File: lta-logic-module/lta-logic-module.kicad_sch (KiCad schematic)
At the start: 14 parts

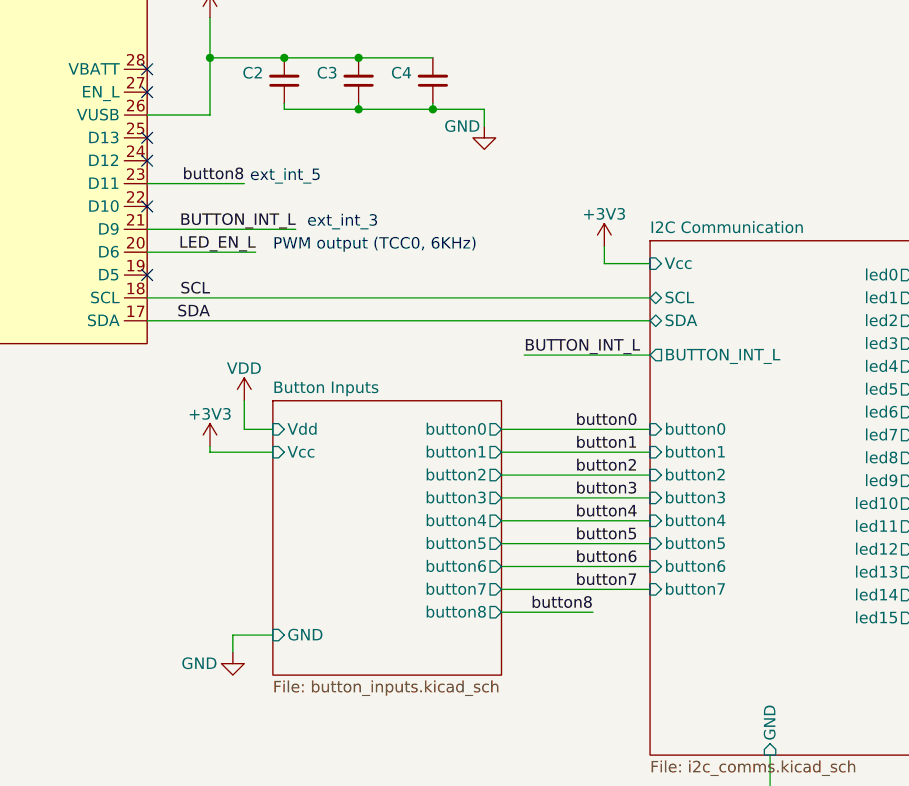
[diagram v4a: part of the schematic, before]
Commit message: Relocated optosensor to south side of board.
* Moved optosensor logic away from the USB plug-side of the Feather.
  You can now plug in USB while the Feather is attached to the board.
* Changed schematic such that `button0` now goes directly to the
  Feather; buttons 1--8 are on the I2C bus. Cleans up some obnoxious
  routing.
* Optimized other routing & GND fill.
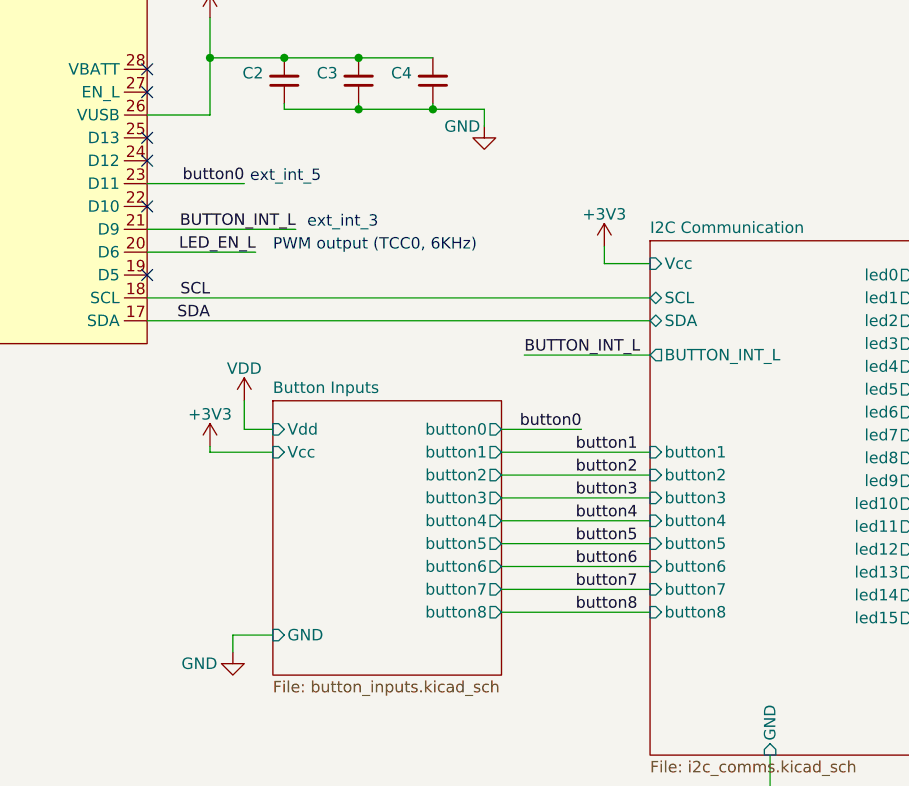
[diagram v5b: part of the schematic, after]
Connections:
- net button0: now also U1.23 (D11)
- net button8: no longer U1.23 (D11)
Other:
- sheet I2C Communication ports: added button8; removed button0
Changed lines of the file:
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@@
-    (stroke (width 0) (type default) (color 0 0 0 0))
-  )
-  (wire (pts (xy 132.715 111.76) (xy 149.225 111.76))
     (stroke (width 0) (type default) (color 0 0 0 0))
   )
@@
     (stroke (width 0) (type default) (color 0 0 0 0))
   )
+  (wire (pts (xy 132.715 111.76) (xy 141.605 111.76))
+    (stroke (width 0) (type default) (color 0 0 0 0))
+  )
   (wire (pts (xy 139.7 171.45) (xy 139.7 179.07))
     (stroke (width 0) (type default) (color 0 0 0 0))
@@
     (stroke (width 0) (type default) (color 0 0 0 0))
   )
-  (wire (pts (xy 132.715 132.08) (xy 142.875 132.08))
+  (wire (pts (xy 132.715 132.08) (xy 149.225 132.08))
     (stroke (width 0) (type default) (color 0 0 0 0))
   )
@@
     (effects (font (size 1.27 1.27)) (justify left bottom))
   )
-  (label "button8" (at 142.875 132.08 180)
+  (label "button8" (at 140.97 132.08 0)
+    (effects (font (size 1.27 1.27)) (justify left bottom))
+  )
+  (label "button0" (at 141.605 111.76 180)
     (effects (font (size 1.27 1.27)) (justify right bottom))
   )
-  (label "button0" (at 140.97 111.76 0)
-    (effects (font (size 1.27 1.27)) (justify left bottom))
-  )
   (label "button2" (at 140.97 116.84 0)
     (effects (font (size 1.27 1.27)) (justify left bottom))
@@
     (effects (font (size 1.27 1.27)) (justify left bottom))
   )
-  (label "button8" (at 104.14 84.455 180)
+  (label "button0" (at 104.14 84.455 180)
     (effects (font (size 1.27 1.27)) (justify right bottom))
   )
@@
       (effects (font (size 1.27 1.27)) (justify left))
     )
-    (pin "button0" input (at 149.225 111.76 180)
-      (effects (font (size 1.27 1.27)) (justify left))
-    )
     (pin "button1" input (at 149.225 114.3 180)
       (effects (font (size 1.27 1.27)) (justify left))
@@
       (effects (font (size 1.27 1.27)) (justify left))
     )
+    (pin "button8" input (at 149.225 132.08 180)
+      (effects (font (size 1.27 1.27)) (justify left))
+    )

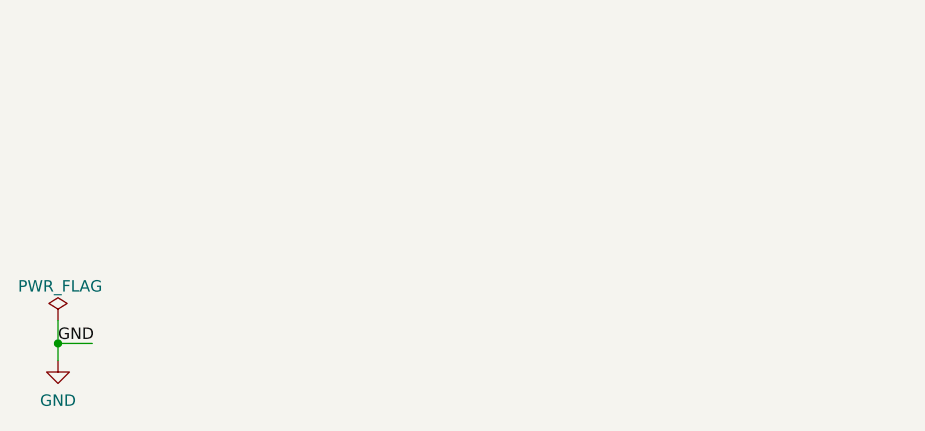
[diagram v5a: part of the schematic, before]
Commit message: Add test points
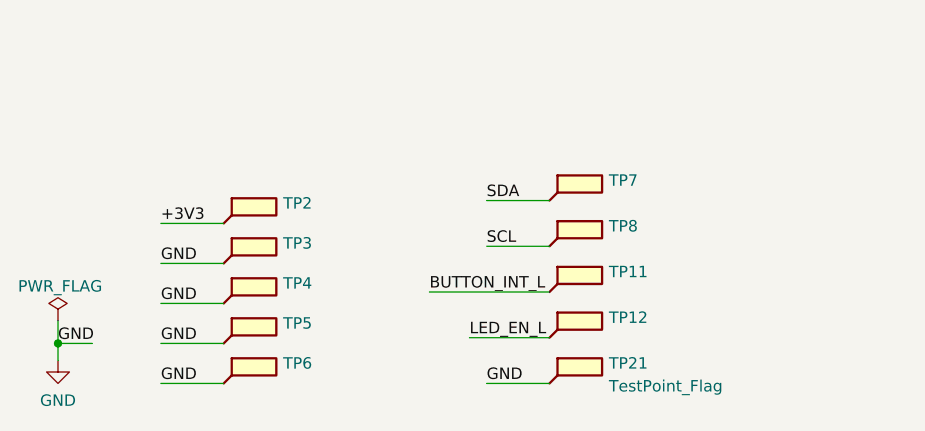
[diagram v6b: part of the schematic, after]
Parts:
- added TP11, TP12, TP2, TP3, TP4, TP5, TP6, TP7, TP8: (no value), symbol Connector:TestPoint_Flag
- added TP21: TestPoint_Flag, Aaron_THT:TestPoint_THTPad_1.0x1.0mm_Drill0.3mm, symbol Connector:TestPoint_Flag
- FID1, FID2, FID3, H1, H2, H3, H4: now left out of the parts list
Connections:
- net +3V3: now also TP2.1
- net BUTTON_INT_L: now also TP11.1
- net GND: now also TP21.1, TP3.1, TP4.1, TP5.1, TP6.1
- net LED_EN_L: now also TP12.1
- net SCL: now also TP8.1
- net SDA: now also TP7.1

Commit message: Final tweaks before RTM.
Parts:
- TP21: value TestPoint_Flag -> (none); footprint Aaron_THT:TestPoint_THTPad_1.0x1.0mm_Drill0.3mm -> (none)
- U1: Comment Use 1x16 and 1x12 female THT headers 2.54mm pitch -> Use 1x16 and 1x12 female THT headers 2.54mm pitch, 6.5--8.0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
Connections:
- net LED_EN_L renamed LED_EN
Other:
- sheet LED Signal Outputs ports: added LED_EN; removed LED_EN_L
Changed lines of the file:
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@@
     (stroke (width 0) (type default) (color 0 0 0 0))
   )
-  (wire (pts (xy 93.345 92.075) (xy 105.41 92.075))
+  (wire (pts (xy 93.345 92.075) (xy 103.505 92.075))
     (stroke (width 0) (type default) (color 0 0 0 0))
   )
@@
     (effects (font (size 1.27 1.27)) (justify left bottom))
   )
-  (label "LED_EN_L" (at 182.245 142.24 0)
+  (label "LED_EN" (at 182.245 142.24 0)
     (effects (font (size 1.27 1.27)) (justify left bottom))
   )
@@
     (effects (font (size 1.27 1.27)) (justify right bottom))
   )
-  (label "LED_EN_L" (at 63.5 189.865 0)
+  (label "LED_EN" (at 63.5 189.865 0)
     (effects (font (size 1.27 1.27)) (justify left bottom))
   )
@@
     (effects (font (size 1.27 1.27)) (justify left bottom))
   )
-  (label "LED_EN_L" (at 105.41 92.075 180)
+  (label "LED_EN" (at 103.505 92.075 180)
     (effects (font (size 1.27 1.27)) (justify right bottom))
   )
@@
       (effects (font (size 1.27 1.27)) (justify left))
     )
-    (property "Value" "TestPoint_Flag" (id 1) (at 78.994 195.2502 0)
-      (effects (font (size 1.27 1.27)) (justify left))
-    )
-    (property "Footprint" "Aaron_THT:TestPoint_THTPad_1.0x1.0mm_Drill0.3mm" (id 2) (at 77.47 194.945 0)
+    (property "Value" "" (id 1) (at 78.994 195.2502 0)
+      (effects (font (size 1.27 1.27)) (justify left))
+    )
+    (property "Footprint" "" (id 2) (at 77.47 194.945 0)
       (effects (font (size 1.27 1.27)) hide)
     )
@@
       (effects (font (size 1.27 1.27)) hide)
     )
-    (property "Comment" "Use 1x16 and 1x12 female THT headers 2.54mm pitch" (id 4) (at 64.135 59.055 0)
+    (property "Comment" "Use 1x16 and 1x12 female THT headers 2.54mm pitch, 6.5--8.0mm tall" (id 4) (at 64.135 59.055 0)
       (effects (font (size 1.27 1.27)) hide)
     )
@@
       (effects (font (size 1.27 1.27)) (justify left))
     )
-    (pin "LED_EN_L" input (at 193.675 142.24 180)
-      (effects (font (size 1.27 1.27)) (justify left))
-    )
+    (pin "LED_EN" input (at 193.675 142.24 180)
+      (effects (font (size 1.27 1.27)) (justify left))
+    )

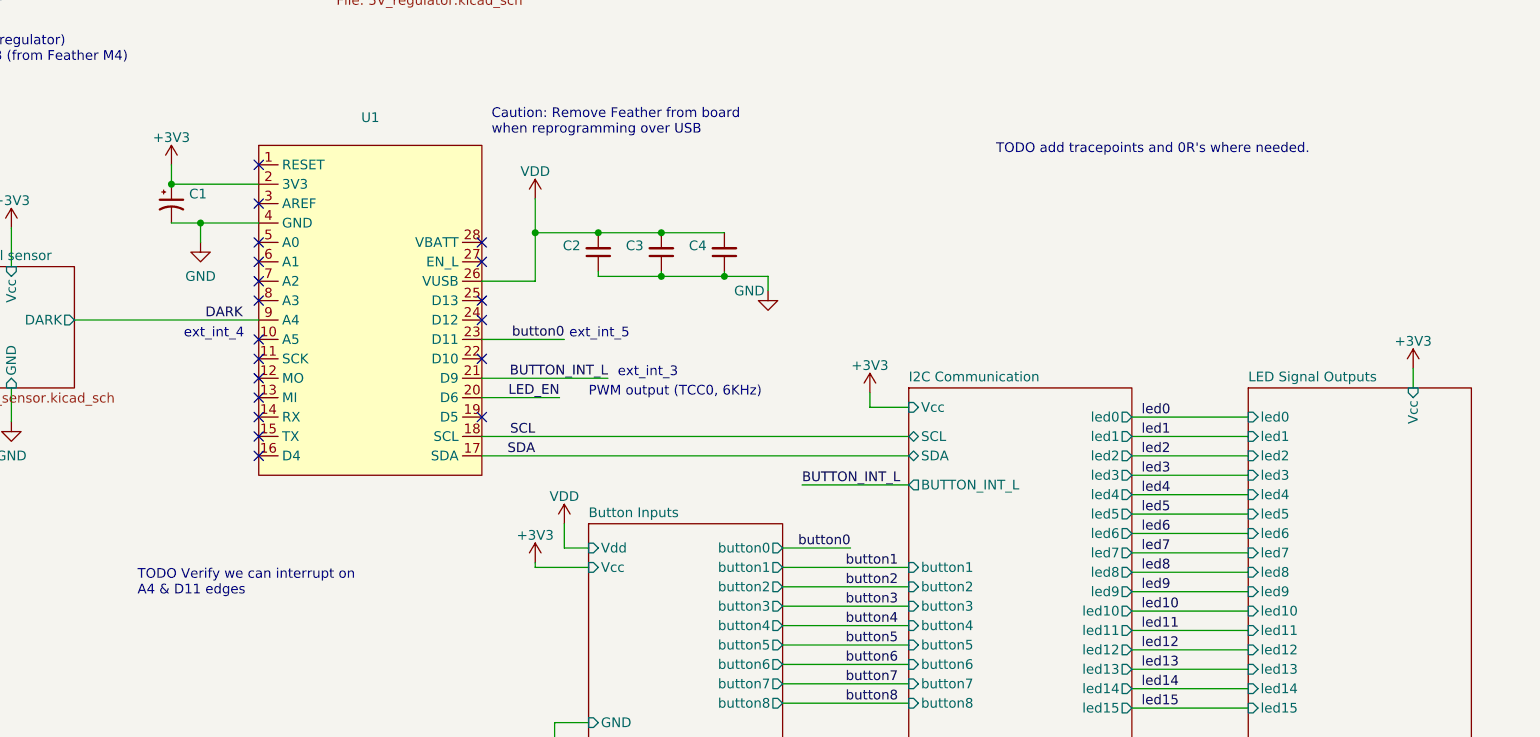
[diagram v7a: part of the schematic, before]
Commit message: Fix GND path return.
* Route power traces over ground plane.
* Add routed corners to edge cuts
* Remove final TODO notes.
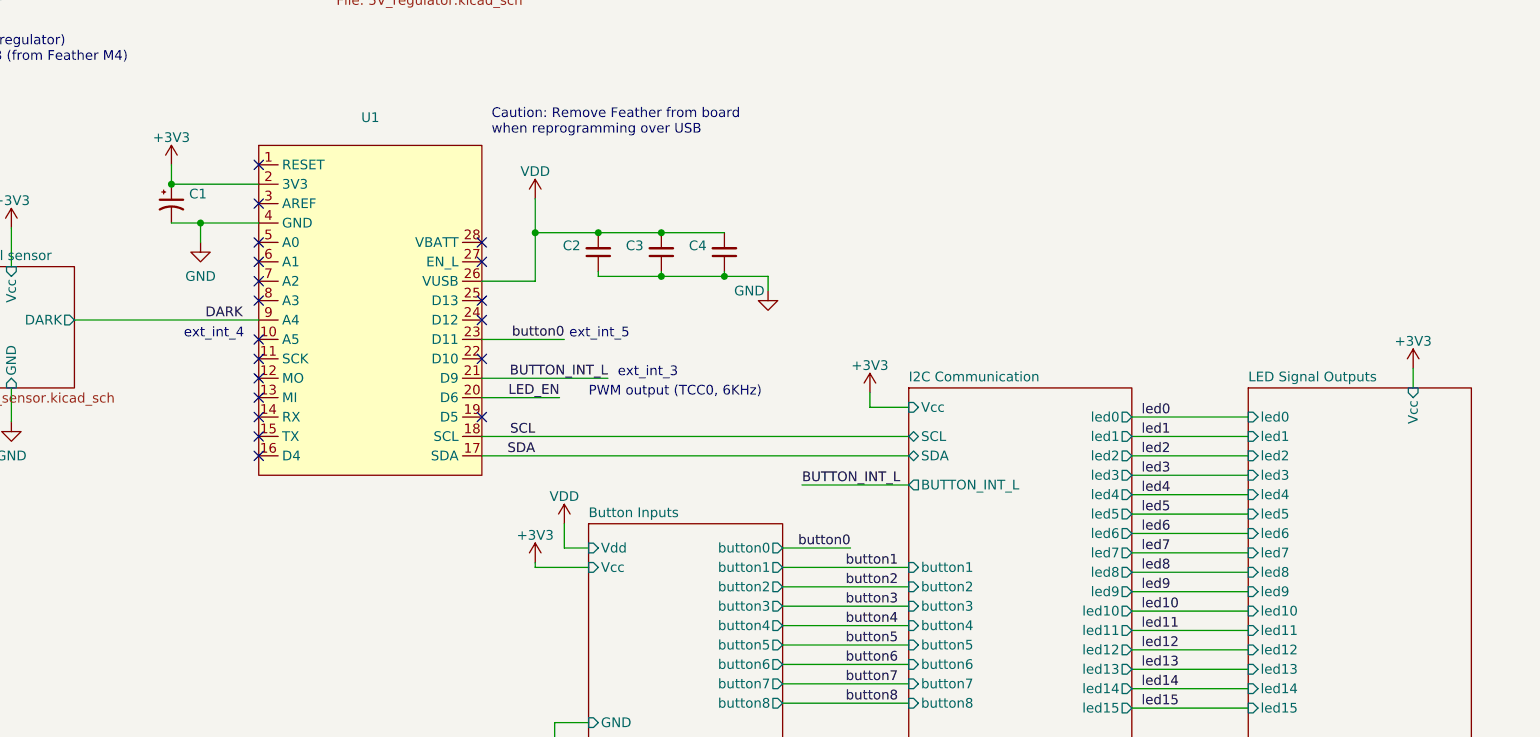
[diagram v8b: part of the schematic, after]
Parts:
- C1: Comment 22u AVX TPS 25V low-ESR solid tantalum; exact MPN -> 22u 10% >=16V 7343 ESR<=250mOhm solid tantalum
- J1: Comment (none) -> Molex Micro-Fit 3 2-pin
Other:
- note removed: "TODO Verify we can interrupt on A4 & D11 edges"
- note removed: "TODO add tracepoints and 0R's where needed."
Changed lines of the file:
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@@
     (stroke (width 0) (type default) (color 0 0 0 0))
-  )
-  (text "TODO add tracepoints and 0R's where needed." (at 160.655 60.325 0)
-    (effects (font (size 1.27 1.27)) (justify left bottom))
   )
   (text "ext_int_5\n" (at 104.775 84.455 0)
@@
   )
   (text "Use M2 screws for mounting holes " (at 132.715 165.1 0)
-    (effects (font (size 1.27 1.27)) (justify left bottom))
-  )
-  (text "TODO Verify we can interrupt on\nA4 & D11 edges" (at 48.26 118.11 0)
     (effects (font (size 1.27 1.27)) (justify left bottom))
   )
@@
       (effects (font (size 1.524 1.524)) hide)
     )
-    (property "Comment" "" (id 4) (at 27.94 22.86 0)
+    (property "Comment" "Molex Micro-Fit 3 2-pin" (id 4) (at 27.94 22.86 0)
       (effects (font (size 1.27 1.27)) hide)
     )
@@
       (effects (font (size 1.27 1.27)) hide)
     )
-    (property "Comment" "22u AVX TPS 25V low-ESR solid tantalum; exact MPN" (id 6) (at 52.705 66.675 0)
-      (effects (font (size 1.27 1.27)) hide)
-    )
+    (property "Comment" "22u 10% >=16V 7343 ESR<=250mOhm solid tantalum" (id 6) (at 52.705 66.675 0)
+      (effects (font (size 1.27 1.27)) hide)
+    )
